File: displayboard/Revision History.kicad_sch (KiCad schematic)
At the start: 0 parts

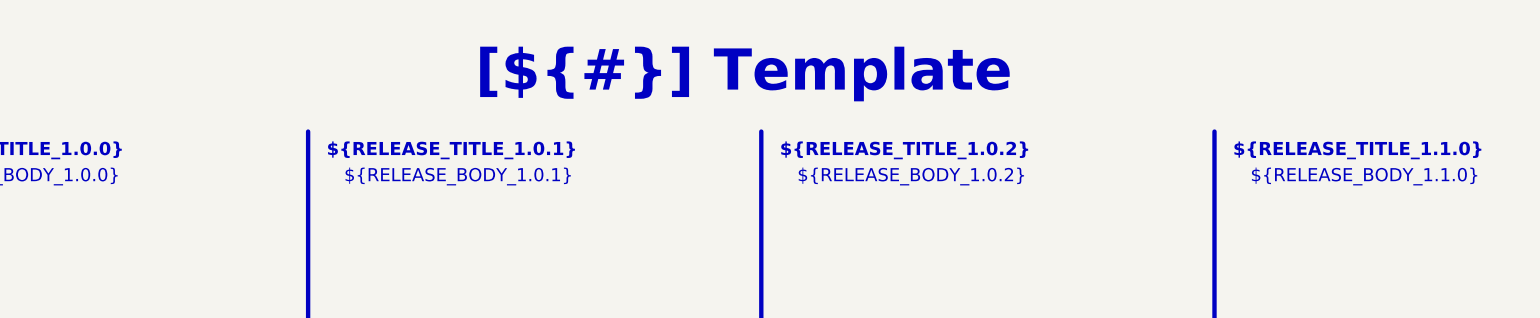
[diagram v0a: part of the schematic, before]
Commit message: Remove old production files, add cutout for the programming cable, add connector for mainboard cable
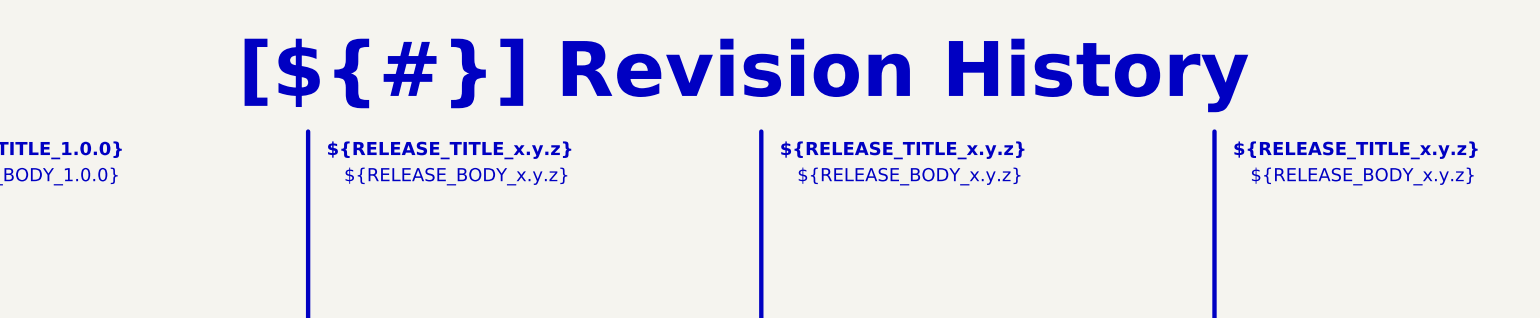
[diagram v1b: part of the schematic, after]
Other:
- title: Template -> Revision History
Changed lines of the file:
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@@
 	(paper "A4")
 	(title_block
-		(title "Template")
+		(title "Revision History")
 		(date "2025-12-19")
 		(rev "1")
 		(company "${COMPANY}")
 	)
-	(text_box "${RELEASE_BODY_1.1.0}"
+	(text_box "${RELEASE_BODY_x.y.z}"
 		(exclude_from_sim no)
 		(at 220.98 35.56 0)
@@
 		(stroke
 			(width -0.0001)
-			(type default)
+			(type solid)
 		)
 		(fill
@@
 			)
 			(justify left top)
-		)
-	)
-	(text_box "[${#}] ${TITLE}"
-		(exclude_from_sim no)
-		(at 80.01 16.51 0)
-		(size 137.16 12.7)
-		(margins 4.4999 4.4999 4.4999 4.4999)
-		(stroke
-			(width -0.0001)
-			(type default)
-		)
-		(fill
-			(type none)
-		)
-		(effects
-			(font
-				(face "Times New Roman")
-				(size 6 6)
-				(thickness 1.2)
-				(bold yes)
-				(color 162 22 34 1)
-			)
 		)
 	)
@@
 		)
 	)
-	(text_box "${RELEASE_TITLE_1.0.2}"
+	(text_box "[${#}] ${TITLE}"
+		(exclude_from_sim no)
+		(at 12.7 12.7 0)
+		(size 271.78 20.32)
+		(margins 5.9999 5.9999 5.9999 5.9999)
+		(stroke
+			(width -0.0001)
+			(type default)
+		)
+		(fill
+			(type none)
+		)
+		(effects
+			(font
+				(face "Times New Roman")
+				(size 8 8)
+				(thickness 1.2)
+				(bold yes)
+				(color 162 22 34 1)
+			)
+		)
+	)
+	(text_box "${RELEASE_TITLE_x.y.z}"
 		(exclude_from_sim no)
 		(at 152.4 31.75 0)
@@
 		(stroke
 			(width -0.0001)
-			(type default)
+			(type solid)
 		)
 		(fill
@@
 		)
 	)
-	(text_box "${RELEASE_BODY_1.0.2}"
+	(text_box "${RELEASE_BODY_x.y.z}"
 		(exclude_from_sim no)
 		(at 154.94 35.56 0)
@@
 		(stroke
 			(width -0.0001)
-			(type default)
+			(type solid)
 		)
 		(fill
@@
 		)
 	)
-	(text_box "${RELEASE_BODY_1.0.1}"
+	(text_box "${RELEASE_BODY_x.y.z}"
 		(exclude_from_sim no)
 		(at 88.9 35.56 0)
@@
 		(stroke
 			(width -0.0001)
-			(type default)
+			(type solid)
 		)
 		(fill
@@
 		)
 	)
-	(text_box "${RELEASE_TITLE_1.0.1}"
+	(text_box "${RELEASE_TITLE_x.y.z}"
 		(exclude_from_sim no)
 		(at 86.36 31.75 0)
@@
 		(stroke
 			(width -0.0001)
-			(type default)
+			(type solid)
 		)
 		(fill
@@
 		)
 	)
-	(text_box "${RELEASE_TITLE_1.1.0}"
+	(text_box "${RELEASE_TITLE_x.y.z}"
 		(exclude_from_sim no)
 		(at 218.44 31.75 0)
@@
 		(stroke
 			(width -0.0001)
-			(type default)
+			(type solid)
 		)
 		(fill
